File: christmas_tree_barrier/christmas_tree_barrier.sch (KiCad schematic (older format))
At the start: 1 part

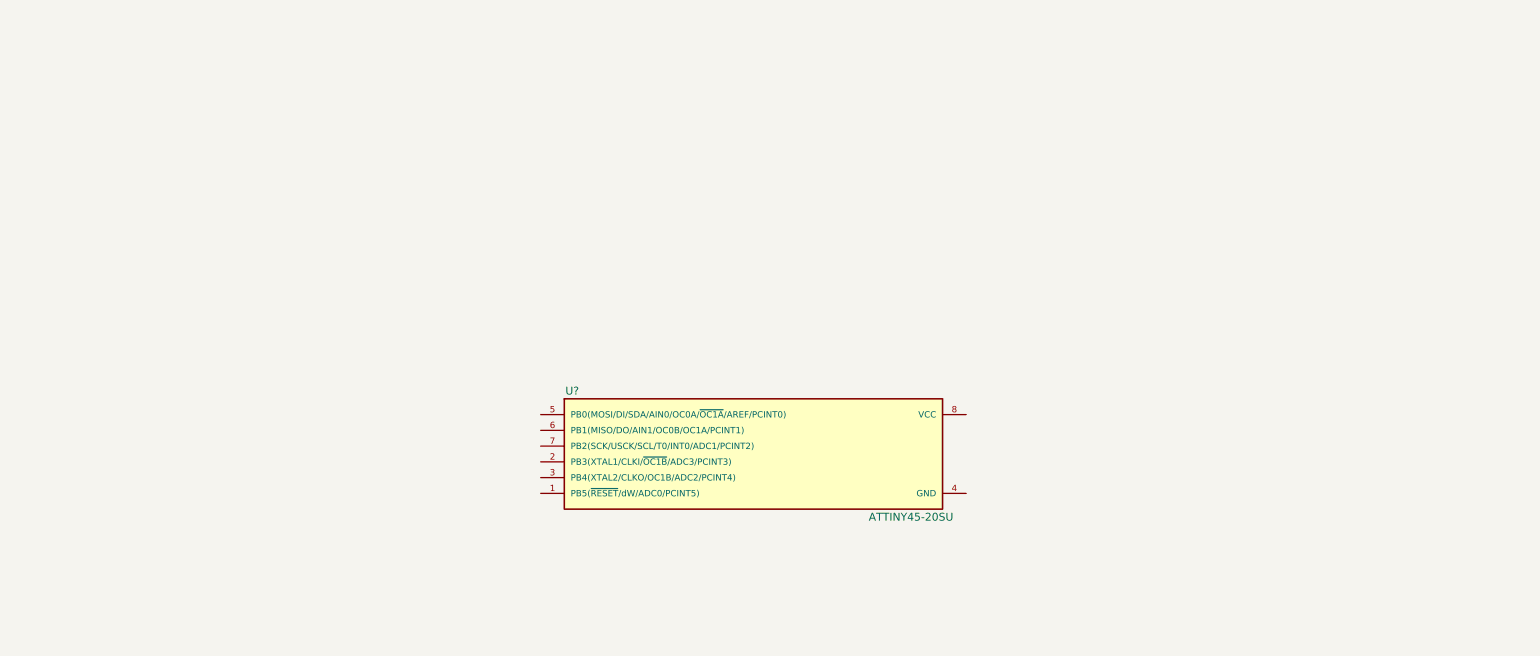
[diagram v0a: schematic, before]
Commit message: Finished new schematic; started pcb layout
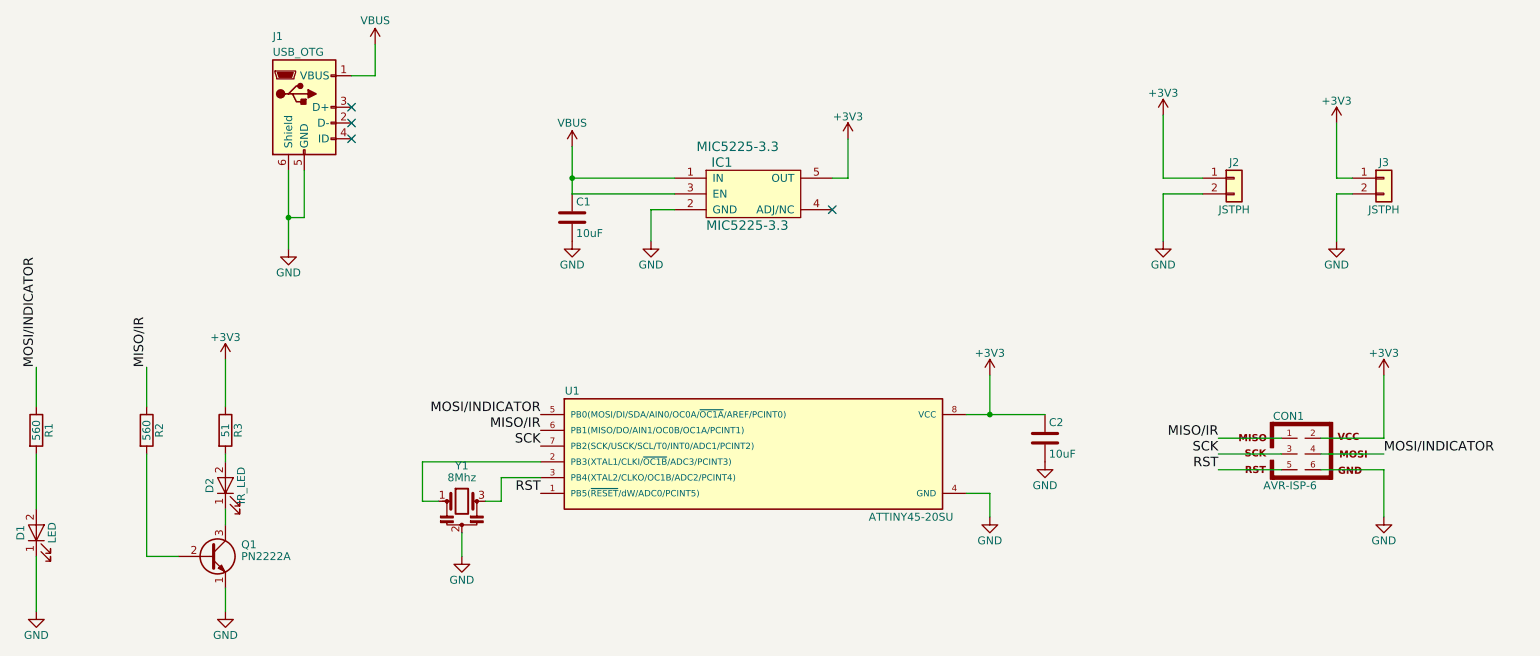
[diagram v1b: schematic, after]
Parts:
- added C1, C2: 10uF, Capacitors_SMD:C_1206, symbol C
- added CON1: AVR-ISP-6, Pin_Headers:Pin_Header_Straight_2x03_Pitch2.54mm, symbol AVR-ISP-6
- added D1: LED, LEDs:LED_1206, symbol LED
- added D2: IR_LED, LEDs:LED_0603_HandSoldering, symbol LED
- added IC1: MIC5225-3.3, TO_SOT_Packages_SMD:SOT-23-5_HandSoldering, symbol MIC5225-3.3
- added J1: USB_OTG, NurseryPager-Hardware:USB_Micro-B_10103594-0001LF, symbol USB_OTG
- added J2, J3: JSTPH, Connectors_JST:JST_PH_B2B-PH-SM4-TB_02x2.00mm_Straight, symbol Conn_01x02
- added Q1: PN2222A, TO_SOT_Packages_SMD:SOT-23, symbol PN2222A
- added R1, R2: 560, Resistors_SMD:R_1206, symbol R
- added R3: 51, Resistors_SMD:R_1206, symbol R
- added Y1: 8Mhz, Crystals:Resonator_SMD-3pin_7.2x3.0mm_HandSoldering, symbol Resonator
- gave numbers to parts that had none: 1
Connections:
- net RST: now reaches U1.1 (PB5(~RESET~/dW/ADC0/PCINT5))
- net RST: now also CON1.5
- net at U1.2 (PB3(XTAL1/CLKI/~OC1B~/ADC3/PCINT3)): now also Y1.1
- net at U1.3 (PB4(XTAL2/CLKO/OC1B/ADC2/PCINT4)): now also Y1.3
- net GND: now reaches U1.4 (GND)
- net GND: now also C1.2, C2.2, CON1.6, D1.1 (K), IC1.2 (GND), J1.5 (GND), J1.6 (Shield), J2.2 (Pin_2), J3.2 (Pin_2), Q1.1 (E), Y1.2
- net MOSI/INDICATOR: now reaches U1.5 (PB0(MOSI/DI/SDA/AIN0/OC0A/~OC1A~/AREF/PCINT0))
- net MOSI/INDICATOR: now also CON1.4, R1.1
- net MISO/IR: now reaches U1.6 (PB1(MISO/DO/AIN1/OC0B/OC1A/PCINT1))
- net MISO/IR: now also CON1.1, R2.1
- net SCK: now reaches U1.7 (PB2(SCK/USCK/SCL/T0/INT0/ADC1/PCINT2))
- net SCK: now also CON1.3
- net +3V3: now reaches U1.8 (VCC)
- net +3V3: now also C2.1, CON1.2, IC1.5 (OUT), J2.1 (Pin_1), J3.1 (Pin_1), R3.1
- new net: D1.2 (A), R1.2
- new net: Q1.2 (B), R2.2
- new net: D2.2 (A), R3.2
- new net: D2.1 (K), Q1.3 (C)
- new net VBUS: C1.1, IC1.1 (IN), IC1.3 (EN), J1.1 (VBUS)
- no-connect marks 0 -> 4

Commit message: Working on new pcb
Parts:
- removed Q1: PN2222A, TO_SOT_Packages_SMD:SOT-23, symbol PN2222A
- added Q1: Q_PNP_BEC, TO_SOT_Packages_SMD:SOT-23_Handsoldering, symbol Q_PNP_BEC
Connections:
- net GND: now also Q1.2 (E)
- net at R2.2: now also Q1.1 (B)
- net at D2.1 (K): now also Q1.3 (C)
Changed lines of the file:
@@
-$EndComp
-$Comp
-L PN2222A Q1
-U 1 1 5A1C670A
-P 2350 4350
-F 0 "Q1" H 2550 4425 50  0000 L CNN
-F 1 "PN2222A" H 2550 4350 50  0000 L CNN
-F 2 "TO_SOT_Packages_SMD:SOT-23" H 2550 4275 50  0001 L CIN
-F 3 "" H 2350 4350 50  0001 L CNN
-	1    2350 4350
-	1    0    0    -1
 $EndComp
 $Comp
@@
 Wire Wire Line
 	8400 1950 8650 1950
+$Comp
+L Q_PNP_BEC Q1
+U 1 1 5A1CDA3E
+P 2350 4350
+F 0 "Q1" H 2550 4400 50  0000 L CNN
+F 1 "Q_PNP_BEC" H 2550 4300 50  0000 L CNN
+F 2 "TO_SOT_Packages_SMD:SOT-23_Handsoldering" H 2550 4450 50  0001 C CNN
+F 3 "" H 2350 4350 50  0001 C CNN
+	1    2350 4350
+	1    0    0    -1
+$EndComp
 $EndSCHEMATC

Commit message: Mostly finalize placement and outline
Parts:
- Y1: footprint Crystals:Resonator_SMD-3pin_7.2x3.0mm_HandSoldering -> kicad-libs:Resonator_SMD_muRata_CSTCE_G-3pin_3.0x0.7mm
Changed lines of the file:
@@
 RST
 $Comp
-L GND #PWR12
+L GND #PWR01
 U 1 1 5A1C62BB
 P 7300 4100
-F 0 "#PWR12" H 7300 3850 50  0001 C CNN
+F 0 "#PWR01" H 7300 3850 50  0001 C CNN
 F 1 "GND" H 7300 3950 50  0000 C CNN
 F 2 "" H 7300 4100 50  0001 C CNN
@@
 $EndComp
 $Comp
-L +3V3 #PWR11
+L +3V3 #PWR02
 U 1 1 5A1C6304
 P 7300 3200
-F 0 "#PWR11" H 7300 3050 50  0001 C CNN
+F 0 "#PWR02" H 7300 3050 50  0001 C CNN
 F 1 "+3V3" H 7300 3340 50  0000 C CNN
 F 2 "" H 7300 3200 50  0001 C CNN
@@
 F 0 "Y1" H 3950 4225 50  0000 C CNN
 F 1 "8Mhz" H 3950 4150 50  0000 C CNN
-F 2 "Crystals:Resonator_SMD-3pin_7.2x3.0mm_HandSoldering" H 3925 4000 50  0001 C CNN
+F 2 "kicad-libs:Resonator_SMD_muRata_CSTCE_G-3pin_3.0x0.7mm" H 3925 4000 50  0001 C CNN
 F 3 "" H 3925 4000 50  0001 C CNN
 	1    3950 4000
@@
 $EndComp
 $Comp
-L GND #PWR6
+L GND #PWR03
 U 1 1 5A1C63A0
 P 3950 4350
-F 0 "#PWR6" H 3950 4100 50  0001 C CNN
+F 0 "#PWR03" H 3950 4100 50  0001 C CNN
 F 1 "GND" H 3950 4200 50  0000 C CNN
 F 2 "" H 3950 4350 50  0001 C CNN
@@
 $EndComp
 $Comp
-L +3V3 #PWR2
+L +3V3 #PWR04
 U 1 1 5A1C6749
 P 2450 3100
-F 0 "#PWR2" H 2450 2950 50  0001 C CNN
+F 0 "#PWR04" H 2450 2950 50  0001 C CNN
 F 1 "+3V3" H 2450 3240 50  0000 C CNN
 F 2 "" H 2450 3100 50  0001 C CNN
@@
 $EndComp
 $Comp
-L GND #PWR1
+L GND #PWR05
 U 1 1 5A1C676D
 P 1250 4700
-F 0 "#PWR1" H 1250 4450 50  0001 C CNN
+F 0 "#PWR05" H 1250 4450 50  0001 C CNN
 F 1 "GND" H 1250 4550 50  0000 C CNN
 F 2 "" H 1250 4700 50  0001 C CNN
@@
 $EndComp
 $Comp
-L GND #PWR3
+L GND #PWR06
 U 1 1 5A1C6791
 P 2450 4700
-F 0 "#PWR3" H 2450 4450 50  0001 C CNN
+F 0 "#PWR06" H 2450 4450 50  0001 C CNN
 F 1 "GND" H 2450 4550 50  0000 C CNN
 F 2 "" H 2450 4700 50  0001 C CNN
@@
 RST
 $Comp
-L +3V3 #PWR18
+L +3V3 #PWR07
 U 1 1 5A1C7024
 P 9800 3200
-F 0 "#PWR18" H 9800 3050 50  0001 C CNN
+F 0 "#PWR07" H 9800 3050 50  0001 C CNN
 F 1 "+3V3" H 9800 3340 50  0000 C CNN
 F 2 "" H 9800 3200 50  0001 C CNN
@@
 $EndComp
 $Comp
-L GND #PWR19
+L GND #PWR08
 U 1 1 5A1C704A
 P 9800 4100
-F 0 "#PWR19" H 9800 3850 50  0001 C CNN
+F 0 "#PWR08" H 9800 3850 50  0001 C CNN
 F 1 "GND" H 9800 3950 50  0000 C CNN
 F 2 "" H 9800 4100 50  0001 C CNN
@@
 $EndComp
 $Comp
-L +3V3 #PWR10
+L +3V3 #PWR09
 U 1 1 5A1C733F
 P 6400 1700
-F 0 "#PWR10" H 6400 1550 50  0001 C CNN
+F 0 "#PWR09" H 6400 1550 50  0001 C CNN
 F 1 "+3V3" H 6400 1840 50  0000 C CNN
 F 2 "" H 6400 1700 50  0001 C CNN
@@
 NoConn ~ 6300 2150
 $Comp
-L GND #PWR9
+L GND #PWR010
 U 1 1 5A1C7375
 P 5150 2350
-F 0 "#PWR9" H 5150 2100 50  0001 C CNN
+F 0 "#PWR010" H 5150 2100 50  0001 C CNN
 F 1 "GND" H 5150 2200 50  0000 C CNN
 F 2 "" H 5150 2350 50  0001 C CNN
@@
 $EndComp
 $Comp
-L VBUS #PWR7
+L VBUS #PWR011
 U 1 1 5A1C739D
 P 4650 1750
-F 0 "#PWR7" H 4650 1600 50  0001 C CNN
+F 0 "#PWR011" H 4650 1600 50  0001 C CNN
 F 1 "VBUS" H 4650 1900 50  0000 C CNN
 F 2 "" H 4650 1750 50  0001 C CNN
@@
 $EndComp
 $Comp
-L GND #PWR8
+L GND #PWR012
 U 1 1 5A1C75B0
 P 4650 2350
-F 0 "#PWR8" H 4650 2100 50  0001 C CNN
+F 0 "#PWR012" H 4650 2100 50  0001 C CNN
 F 1 "GND" H 4650 2200 50  0000 C CNN
 F 2 "" H 4650 2350 50  0001 C CNN
@@
 $EndComp
 $Comp
-L GND #PWR13
+L GND #PWR013
 U 1 1 5A1C763D
 P 7650 3750
-F 0 "#PWR13" H 7650 3500 50  0001 C CNN
+F 0 "#PWR013" H 7650 3500 50  0001 C CNN
 F 1 "GND" H 7650 3600 50  0000 C CNN
 F 2 "" H 7650 3750 50  0001 C CNN
@@
 $EndComp
 $Comp
-L VBUS #PWR5
+L VBUS #PWR014
 U 1 1 5A1C784B
 P 3400 1100
-F 0 "#PWR5" H 3400 950 50  0001 C CNN
+F 0 "#PWR014" H 3400 950 50  0001 C CNN
 F 1 "VBUS" H 3400 1250 50  0000 C CNN
 F 2 "" H 3400 1100 50  0001 C CNN
@@
 NoConn ~ 3250 1700
 $Comp
-L GND #PWR4
+L GND #PWR015
 U 1 1 5A1C78AC
 P 2850 2400
-F 0 "#PWR4" H 2850 2150 50  0001 C CNN
+F 0 "#PWR015" H 2850 2150 50  0001 C CNN
 F 1 "GND" H 2850 2250 50  0000 C CNN
 F 2 "" H 2850 2400 50  0001 C CNN
@@
 $EndComp
 $Comp
-L +3V3 #PWR16
+L +3V3 #PWR016
 U 1 1 5A1C8065
 P 9500 1600
-F 0 "#PWR16" H 9500 1450 50  0001 C CNN
+F 0 "#PWR016" H 9500 1450 50  0001 C CNN
 F 1 "+3V3" H 9500 1740 50  0000 C CNN
 F 2 "" H 9500 1600 50  0001 C CNN
@@
 $EndComp
 $Comp
-L +3V3 #PWR14
+L +3V3 #PWR017
 U 1 1 5A1C8097
 P 8400 1550
-F 0 "#PWR14" H 8400 1400 50  0001 C CNN
+F 0 "#PWR017" H 8400 1400 50  0001 C CNN
 F 1 "+3V3" H 8400 1690 50  0000 C CNN
 F 2 "" H 8400 1550 50  0001 C CNN
@@
 $EndComp
 $Comp
-L GND #PWR17
+L GND #PWR018
 U 1 1 5A1C8672
 P 9500 2350
-F 0 "#PWR17" H 9500 2100 50  0001 C CNN
+F 0 "#PWR018" H 9500 2100 50  0001 C CNN
 F 1 "GND" H 9500 2200 50  0000 C CNN
 F 2 "" H 9500 2350 50  0001 C CNN
@@
 $EndComp
 $Comp
-L GND #PWR15
+L GND #PWR019
 U 1 1 5A1C86A4
 P 8400 2350
-F 0 "#PWR15" H 8400 2100 50  0001 C CNN
+F 0 "#PWR019" H 8400 2100 50  0001 C CNN
 F 1 "GND" H 8400 2200 50  0000 C CNN
 F 2 "" H 8400 2350 50  0001 C CNN

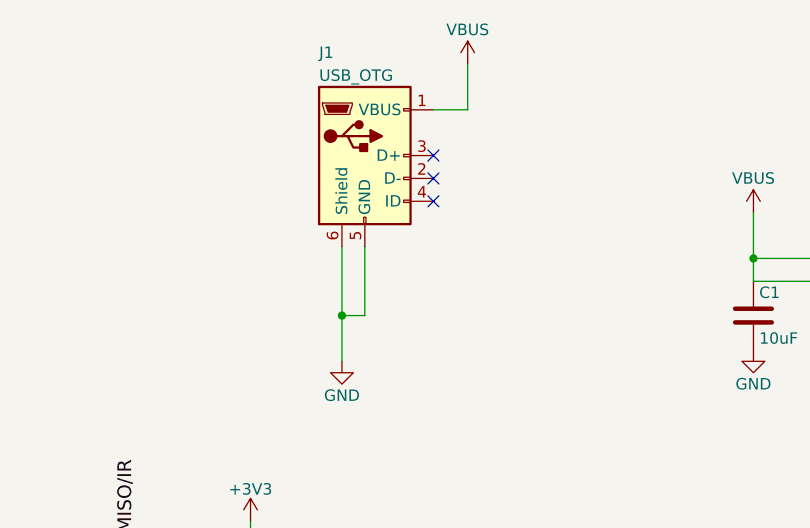
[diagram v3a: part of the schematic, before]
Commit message: Finished layout and routing Also just a bit of silkscreen
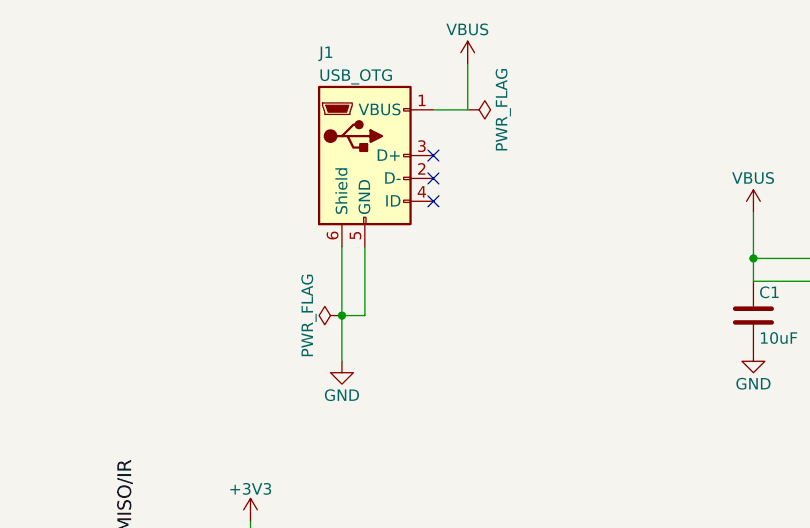
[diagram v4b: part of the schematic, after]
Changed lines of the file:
@@
 	1    0    0    -1
 $EndComp
+$Comp
+L PWR_FLAG #FLG020
+U 1 1 5A1E130D
+P 3400 1300
+F 0 "#FLG020" H 3400 1375 50  0001 C CNN
+F 1 "PWR_FLAG" H 3400 1450 50  0000 C CNN
+F 2 "" H 3400 1300 50  0001 C CNN
+F 3 "" H 3400 1300 50  0001 C CNN
+	1    3400 1300
+	0    1    1    0
+$EndComp
+$Comp
+L PWR_FLAG #FLG021
+U 1 1 5A1E133F
+P 2850 2200
+F 0 "#FLG021" H 2850 2275 50  0001 C CNN
+F 1 "PWR_FLAG" H 2850 2350 50  0000 C CNN
+F 2 "" H 2850 2200 50  0001 C CNN
+F 3 "" H 2850 2200 50  0001 C CNN
+	1    2850 2200
+	0    -1   -1   0
+$EndComp
 $EndSCHEMATC

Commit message: Archive symbols and footprints
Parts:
- C1, C2: footprint Capacitors_SMD:C_1206 -> lib_fp:C_1206
- CON1: footprint Pin_Headers:Pin_Header_Straight_2x03_Pitch2.54mm -> lib_fp:Pin_Header_Straight_2x03_Pitch2.54mm
- D1: footprint LEDs:LED_1206 -> lib_fp:LED_1206
- D2: footprint LEDs:LED_0603_HandSoldering -> lib_fp:LED_0603_HandSoldering
- IC1: footprint TO_SOT_Packages_SMD:SOT-23-5_HandSoldering -> lib_fp:SOT-23-5_HandSoldering
- J1: footprint NurseryPager-Hardware:USB_Micro-B_10103594-0001LF -> lib_fp:USB_Micro-B_10103594-0001LF
- J2, J3: footprint Connectors_JST:JST_PH_B2B-PH-SM4-TB_02x2.00mm_Straight -> lib_fp:JST_PH_B2B-PH-SM4-TB_02x2.00mm_Straight
- Q1: footprint TO_SOT_Packages_SMD:SOT-23_Handsoldering -> lib_fp:SOT-23_Handsoldering
- R1, R2, R3: footprint Resistors_SMD:R_1206 -> lib_fp:R_1206
- U1: footprint Housings_SOIC:SOIC-8_3.9x4.9mm_Pitch1.27mm -> lib_fp:SOIC-8_3.9x4.9mm_Pitch1.27mm
- Y1: footprint kicad-libs:Resonator_SMD_muRata_CSTCE_G-3pin_3.0x0.7mm -> lib_fp:Resonator_SMD_muRata_CSTCE_G-3pin_3.0x0.7mm
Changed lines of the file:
@@
 EESchema Schematic File Version 2
+LIBS:christmas_tree_barrier
 LIBS:power
 LIBS:device
@@
 LIBS:contrib
 LIBS:valves
-LIBS:petezah
-LIBS:petezah-conn
-LIBS:petezah-devices
-LIBS:petezah-ic
-LIBS:petezah-jumpers
-LIBS:petezah-motors
-LIBS:petezah-power
 LIBS:christmas_tree_barrier-cache
 EELAYER 25 0
@@
 Sheet 1 1
 Title "Roomba Christmas Tree Barrier"
-Date "2017-11-26"
+Date "2017-11-30"
 Rev "A"
 Comp "Petezah"
-Comment1 ""
+Comment1 "(C) 2017 Peter Dunshee"
 Comment2 ""
 Comment3 ""
@@
 F 0 "U1" H 4650 4100 50  0000 C CNN
 F 1 "ATTINY45-20SU" H 6800 3300 50  0000 C CNN
-F 2 "Housings_SOIC:SOIC-8_3.9x4.9mm_Pitch1.27mm" H 6750 3700 50  0001 C CIN
+F 2 "lib_fp:SOIC-8_3.9x4.9mm_Pitch1.27mm" H 6750 3700 50  0001 C CIN
 F 3 "" H 5800 3700 50  0001 C CNN
 	1    5800 3700
@@
 F 0 "Y1" H 3950 4225 50  0000 C CNN
 F 1 "8Mhz" H 3950 4150 50  0000 C CNN
-F 2 "kicad-libs:Resonator_SMD_muRata_CSTCE_G-3pin_3.0x0.7mm" H 3925 4000 50  0001 C CNN
+F 2 "lib_fp:Resonator_SMD_muRata_CSTCE_G-3pin_3.0x0.7mm" H 3925 4000 50  0001 C CNN
 F 3 "" H 3925 4000 50  0001 C CNN
 	1    3950 4000
@@
 F 0 "R1" V 1330 3550 50  0000 C CNN
 F 1 "560" V 1250 3550 50  0000 C CNN
-F 2 "Resistors_SMD:R_1206" V 1180 3550 50  0001 C CNN
+F 2 "lib_fp:R_1206" V 1180 3550 50  0001 C CNN
 F 3 "" H 1250 3550 50  0001 C CNN
 	1    1250 3550
@@
 F 0 "R2" V 2030 3550 50  0000 C CNN
 F 1 "560" V 1950 3550 50  0000 C CNN
-F 2 "Resistors_SMD:R_1206" V 1880 3550 50  0001 C CNN
+F 2 "lib_fp:R_1206" V 1880 3550 50  0001 C CNN
 F 3 "" H 1950 3550 50  0001 C CNN
 	1    1950 3550
@@
 F 0 "R3" V 2530 3550 50  0000 C CNN
 F 1 "51" V 2450 3550 50  0000 C CNN
-F 2 "Resistors_SMD:R_1206" V 2380 3550 50  0001 C CNN
+F 2 "lib_fp:R_1206" V 2380 3550 50  0001 C CNN
 F 3 "" H 2450 3550 50  0001 C CNN
 	1    2450 3550
@@
 F 0 "D1" H 1250 4300 50  0000 C CNN
 F 1 "LED" H 1250 4100 50  0000 C CNN
-F 2 "LEDs:LED_1206" H 1250 4200 50  0001 C CNN
+F 2 "lib_fp:LED_1206" H 1250 4200 50  0001 C CNN
 F 3 "" H 1250 4200 50  0001 C CNN
 	1    1250 4200
@@
 F 0 "D2" H 2450 4000 50  0000 C CNN
 F 1 "IR_LED" H 2450 3800 50  0000 C CNN
-F 2 "LEDs:LED_0603_HandSoldering" H 2450 3900 50  0001 C CNN
+F 2 "lib_fp:LED_0603_HandSoldering" H 2450 3900 50  0001 C CNN
 F 3 "" H 2450 3900 50  0001 C CNN
 	1    2450 3900
@@
 F 0 "CON1" H 9195 3940 50  0000 C CNN
 F 1 "AVR-ISP-6" H 9035 3470 50  0000 L BNN
-F 2 "Pin_Headers:Pin_Header_Straight_2x03_Pitch2.54mm" V 8780 3740 50  0001 C CNN
+F 2 "lib_fp:Pin_Header_Straight_2x03_Pitch2.54mm" V 8780 3740 50  0001 C CNN
 F 3 "" H 9275 3700 50  0001 C CNN
 	1    9300 3700
@@
 F 0 "IC1" H 5600 2550 60  0000 C CNN
 F 1 "MIC5225-3.3" H 5500 2150 60  0000 L CNN
-F 2 "TO_SOT_Packages_SMD:SOT-23-5_HandSoldering" H 5750 2200 60  0001 C CNN
+F 2 "lib_fp:SOT-23-5_HandSoldering" H 5750 2200 60  0001 C CNN
 F 3 "" H 5600 2550 60  0001 C CNN
 F 4 "MIC5225-3.3" H 5700 2650 60  0000 C CNN "mfr#"
@@
 F 0 "C1" H 4675 2300 50  0000 L CNN
 F 1 "10uF" H 4675 2100 50  0000 L CNN
-F 2 "Capacitors_SMD:C_1206" H 4688 2050 50  0001 C CNN
+F 2 "lib_fp:C_1206" H 4688 2050 50  0001 C CNN
 F 3 "" H 4650 2200 50  0001 C CNN
 	1    4650 2200
@@
 F 0 "C2" H 7675 3700 50  0000 L CNN
 F 1 "10uF" H 7675 3500 50  0000 L CNN
-F 2 "Capacitors_SMD:C_1206" H 7688 3450 50  0001 C CNN
+F 2 "lib_fp:C_1206" H 7688 3450 50  0001 C CNN
 F 3 "" H 7650 3600 50  0001 C CNN
 	1    7650 3600
@@
 F 0 "J1" H 2750 1950 50  0000 L CNN
 F 1 "USB_OTG" H 2750 1850 50  0000 L CNN
-F 2 "NurseryPager-Hardware:USB_Micro-B_10103594-0001LF" H 3100 1450 50  0001 C CNN
+F 2 "lib_fp:USB_Micro-B_10103594-0001LF" H 3100 1450 50  0001 C CNN
 F 3 "" H 3100 1450 50  0001 C CNN
 	1    2950 1500
@@
 F 0 "J3" H 9800 2050 50  0000 C CNN
 F 1 "JSTPH" H 9800 1750 50  0000 C CNN
-F 2 "Connectors_JST:JST_PH_B2B-PH-SM4-TB_02x2.00mm_Straight" H 9800 1950 50  0001 C CNN
+F 2 "lib_fp:JST_PH_B2B-PH-SM4-TB_02x2.00mm_Straight" H 9800 1950 50  0001 C CNN
 F 3 "" H 9800 1950 50  0001 C CNN
 	1    9800 1950
@@
 F 0 "J2" H 8850 2050 50  0000 C CNN
 F 1 "JSTPH" H 8850 1750 50  0000 C CNN
-F 2 "Connectors_JST:JST_PH_B2B-PH-SM4-TB_02x2.00mm_Straight" H 8850 1950 50  0001 C CNN
+F 2 "lib_fp:JST_PH_B2B-PH-SM4-TB_02x2.00mm_Straight" H 8850 1950 50  0001 C CNN
 F 3 "" H 8850 1950 50  0001 C CNN
 	1    8850 1950
@@
 F 0 "Q1" H 2550 4400 50  0000 L CNN
 F 1 "Q_PNP_BEC" H 2550 4300 50  0000 L CNN
-F 2 "TO_SOT_Packages_SMD:SOT-23_Handsoldering" H 2550 4450 50  0001 C CNN
+F 2 "lib_fp:SOT-23_Handsoldering" H 2550 4450 50  0001 C CNN
 F 3 "" H 2350 4350 50  0001 C CNN
 	1    2350 4350

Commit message: Fix transistor on schematic Accidentally had a PNP instead of an NPN; doesn't change the PCB layout, I just made the mistake on the schematic.
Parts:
- Q1: value Q_PNP_BEC -> Q_NPN_BEC; symbol Q_PNP_BEC -> Q_NPN_BEC
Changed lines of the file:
@@
 	8400 1950 8650 1950
 $Comp
-L Q_PNP_BEC Q1
+L Q_NPN_BEC Q1
 U 1 1 5A1CDA3E
 P 2350 4350
 F 0 "Q1" H 2550 4400 50  0000 L CNN
-F 1 "Q_PNP_BEC" H 2550 4300 50  0000 L CNN
+F 1 "Q_NPN_BEC" H 2550 4300 50  0000 L CNN
 F 2 "lib_fp:SOT-23_Handsoldering" H 2550 4450 50  0001 C CNN
 F 3 "" H 2350 4350 50  0001 C CNN
